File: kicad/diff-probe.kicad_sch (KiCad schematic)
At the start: 34 parts, among them J1 HEADER-1X2CARD-EDGE, J2 Molex 502439-0400, J3 Molex 502494-0470, J4 901-10511-3, U1 OPA847xDBV, U2 OPA847xDBV

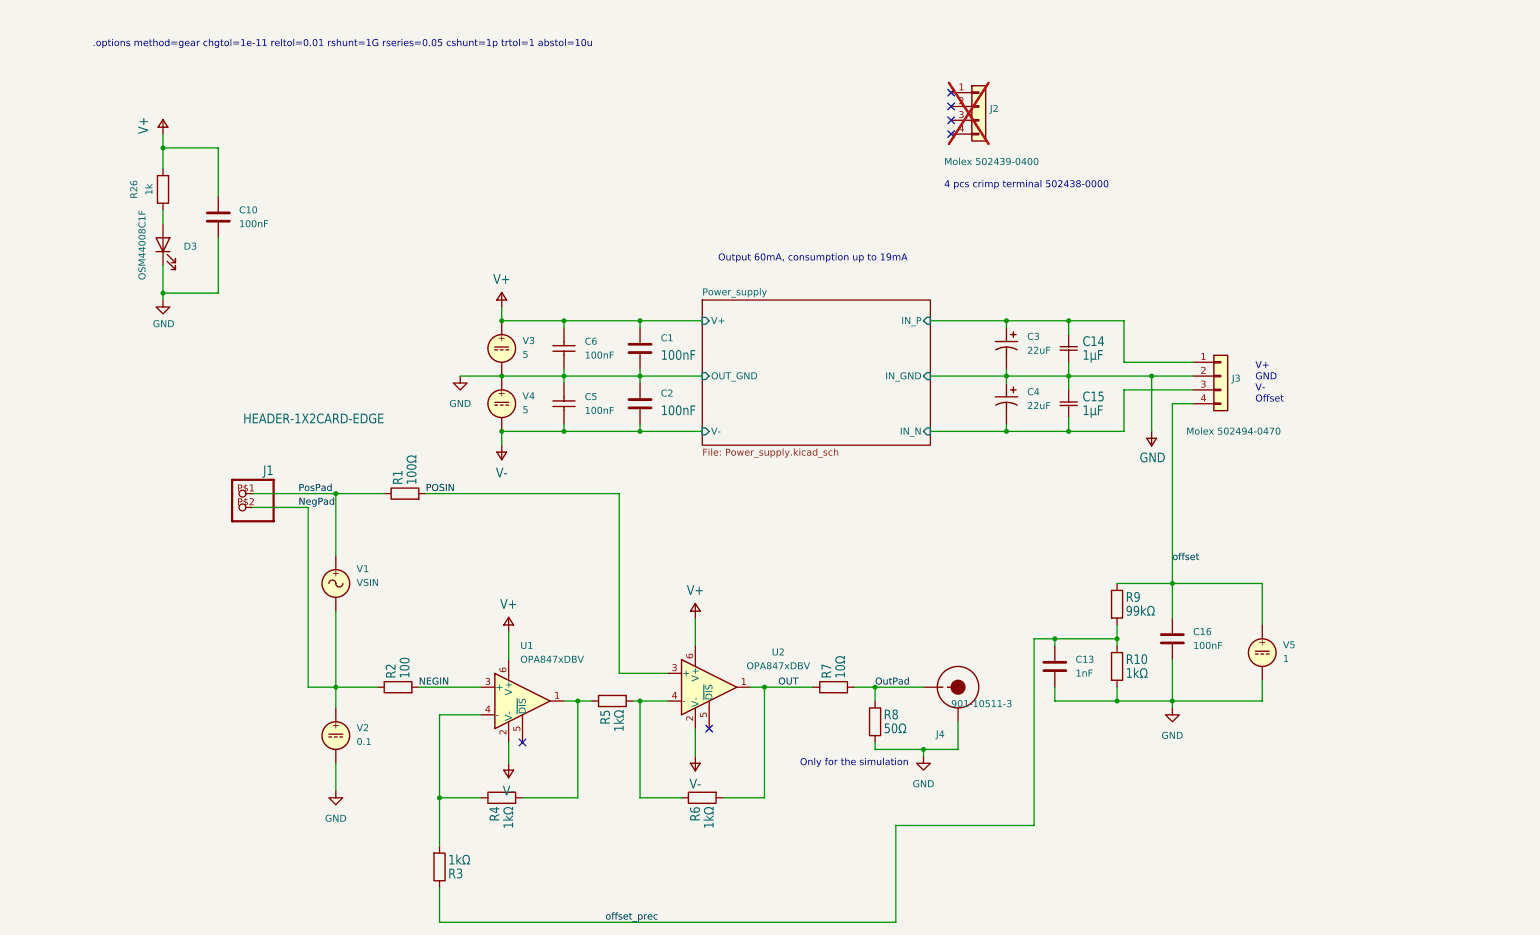
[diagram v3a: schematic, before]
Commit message: Update project. Route signals, make a coplanar 50 R output - two layer board.
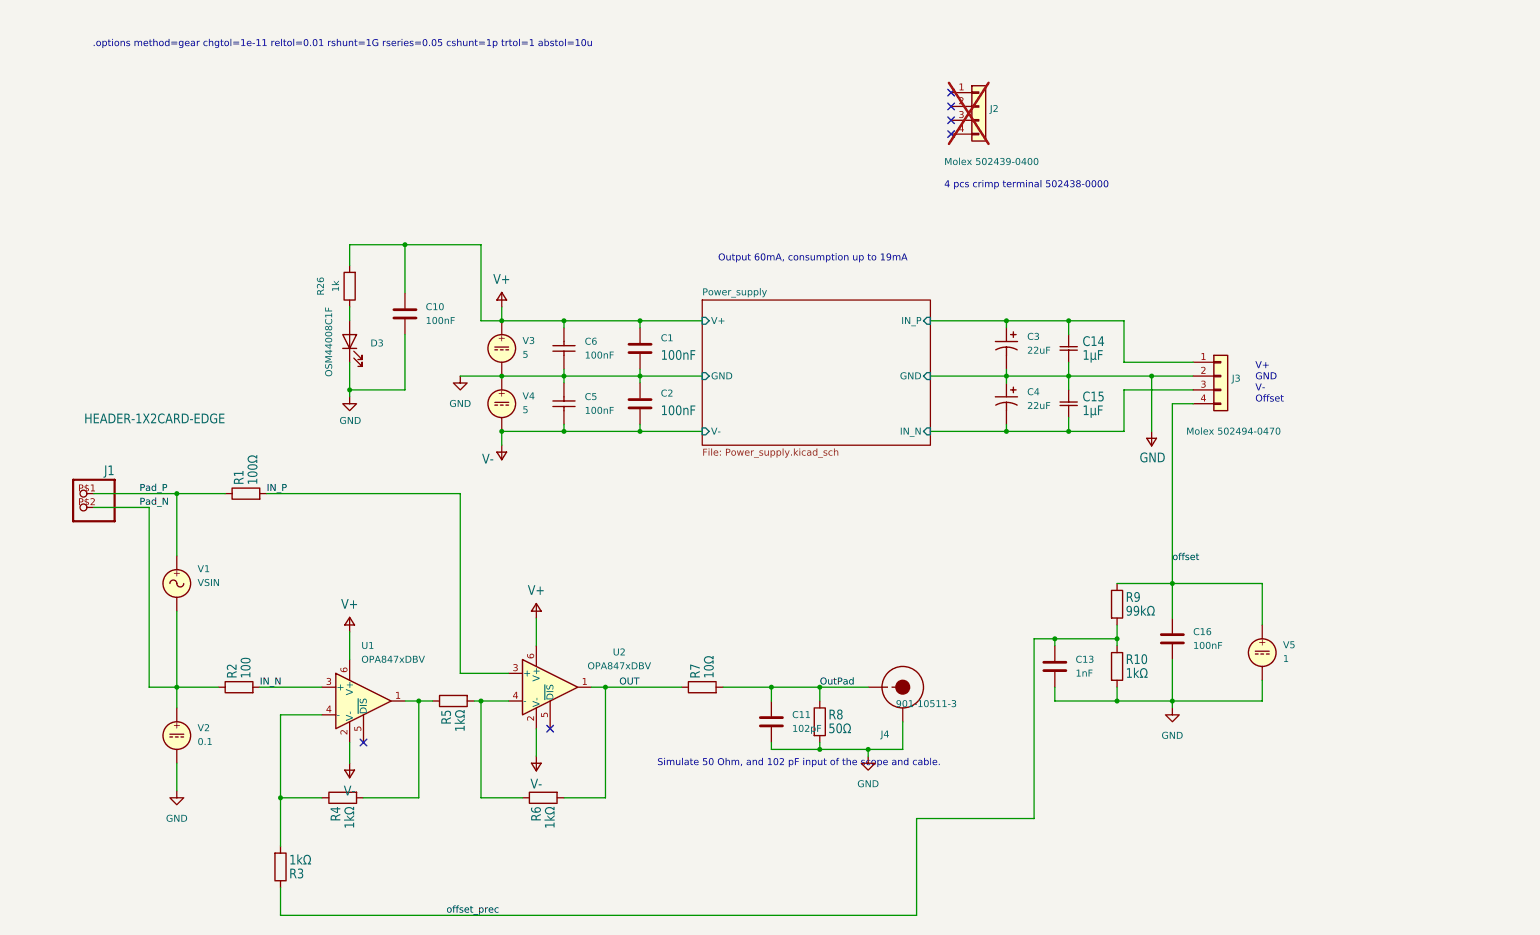
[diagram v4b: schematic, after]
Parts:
- added C11: 102pF, Capacitor_SMD:C_0402_1005Metric, symbol Device:C
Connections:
- net GND: now also C11.2
- net OutPad: now also C11.1
- net Power_supply/V+: now also C10.1, R26.2
- net NEGIN renamed IN_N
- net NegPad renamed Pad_N
- net POSIN renamed IN_P
- net PosPad renamed Pad_P
- net Power_supply/IN_GND renamed Power_supply/GND
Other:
- sheet Power_supply ports: added GND; removed IN_GND, OUT_GND
- note added: "Simulate 50 Ohm, and 102 pF input of the scope and cable."
- note removed: "Only for the simulation"
- moved on the sheet: C10, D3, J1, J4, R1, R2, R26, R3, R4, R5, R6, R7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

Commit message: 1. Update project regarding to the clean up the rules for the https://jlcpcb.com/ 2. Make the output as Co-planar Wave-guide 50 Ohm 3. Trim the differential input length, and width
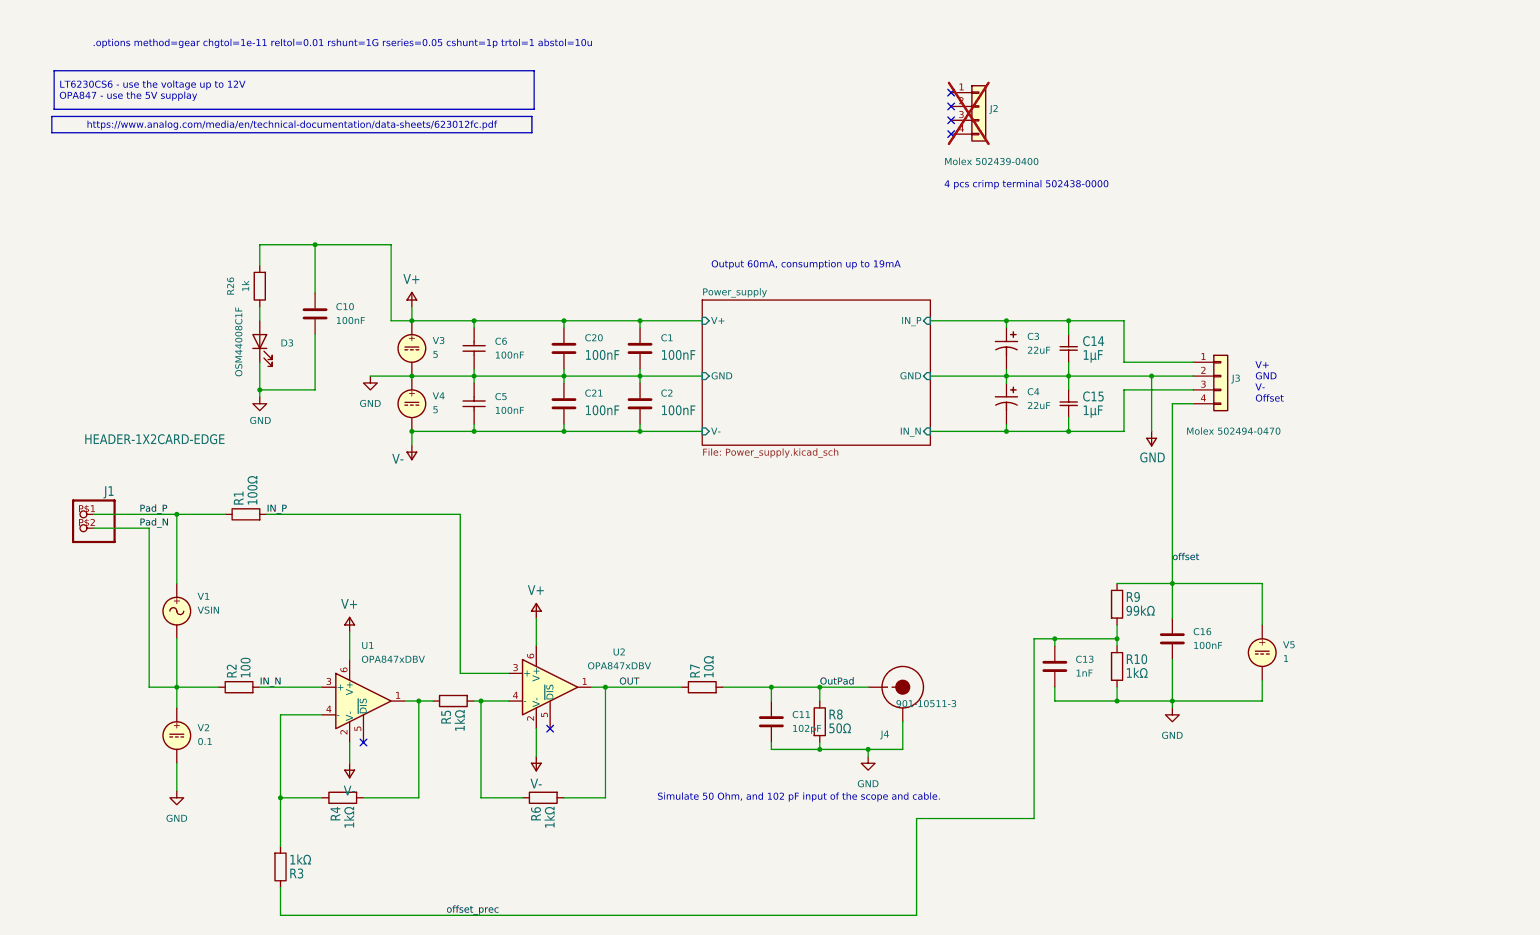
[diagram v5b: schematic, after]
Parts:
- added C20, C21: 100nF, Capacitor_SMD:C_0402_1005Metric, symbol Device:C
- J2, V3, V4, V5: now in the parts list
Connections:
- net GND: now also C20.2, C21.1
- net Power_supply/V+: now also C20.1
- net Power_supply/V-: now also C21.2
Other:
- moved on the sheet: C10, C5, C6, D3, J1, R1, R26, V1, V3, V4

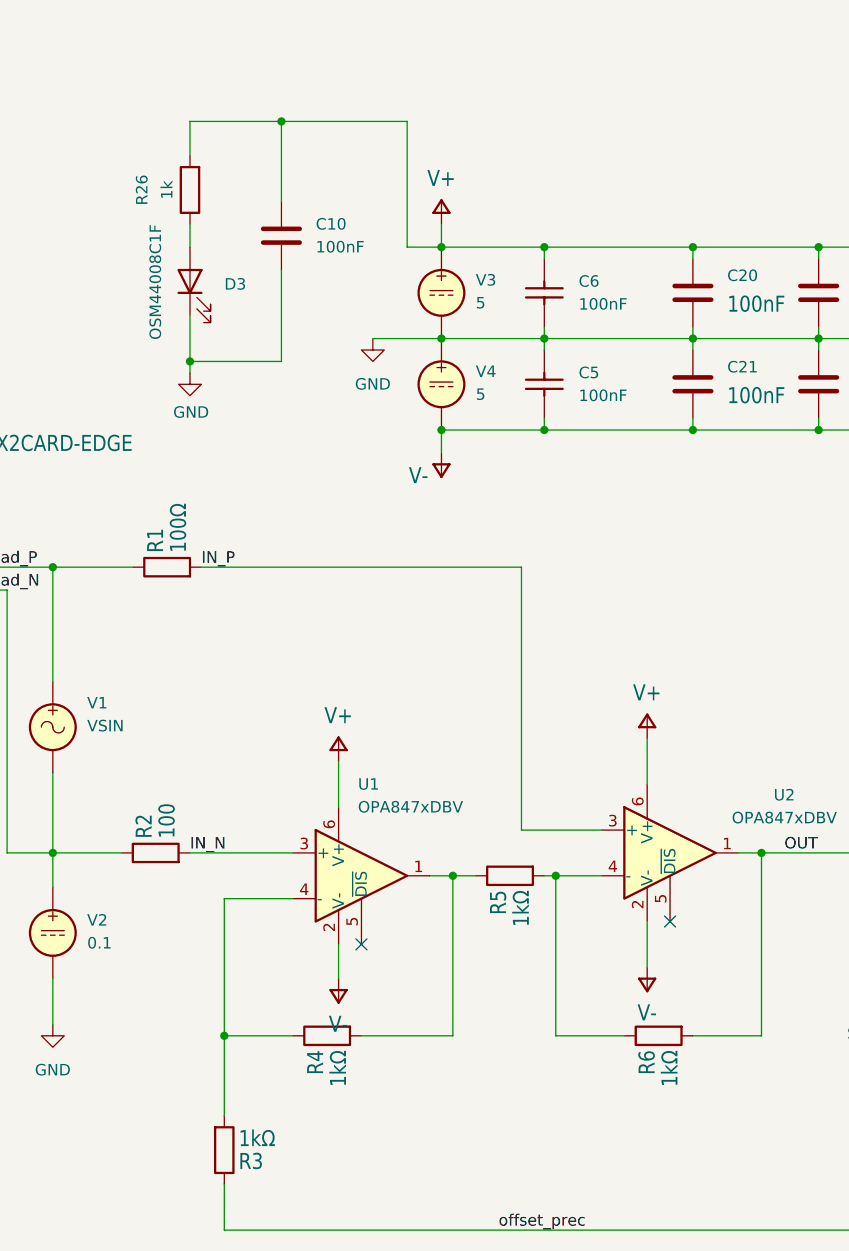
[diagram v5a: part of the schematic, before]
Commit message: Update Autoprobe project to the Kicad 9.xx Add some Bin files for the EEPROM data add some documentation files
Update the High speed diff probe Kicad data
change the silkscreen - more reasonable position
Add the Project Name, an revision on the PCB board.
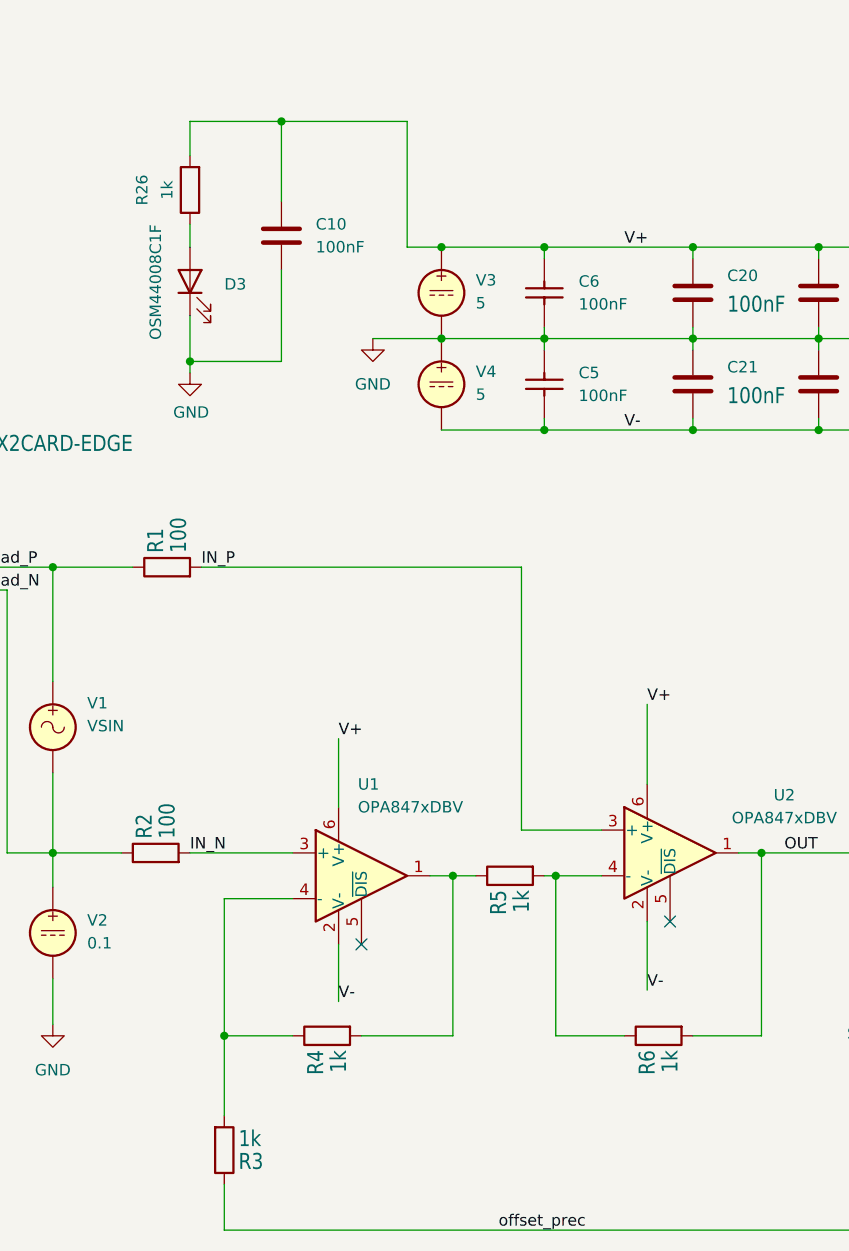
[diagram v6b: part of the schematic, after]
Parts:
- R1: value 100Ω -> 100
- R3, R4, R5, R6: value 1kΩ -> 1k
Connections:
- net Power_supply/V+ is gone; now on net V+: C1.1, C10.1, C20.1, C6.1, R26.2, V3.1
- net Power_supply/V- is gone; now on net V-: C2.2, C21.2, C5.2, V4.2
- net V-: now reaches U2.2 (V-)
- net V-: now also U1.2 (V-)
- net V+: now reaches U2.6 (V+)
- net V+: now also U1.6 (V+)
